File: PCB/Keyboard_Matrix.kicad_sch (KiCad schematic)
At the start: 249 parts

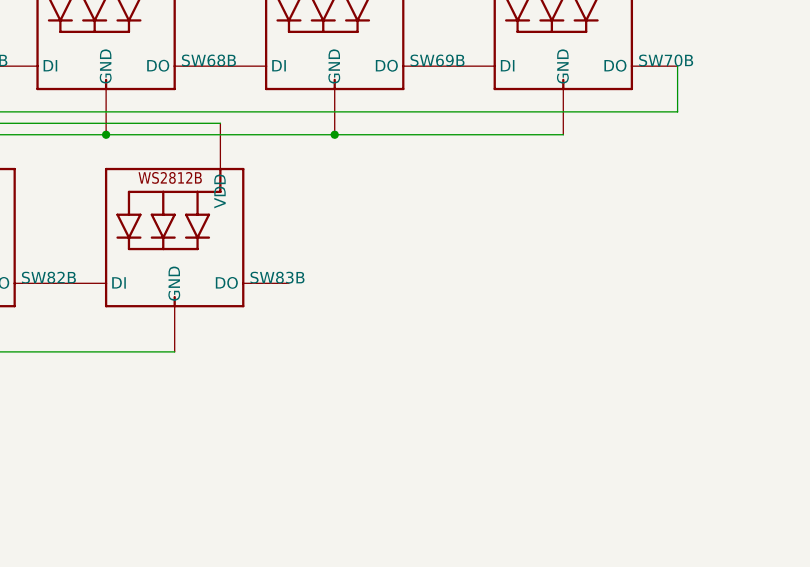
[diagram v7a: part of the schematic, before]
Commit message: PCB is done, still need to do silkscreen
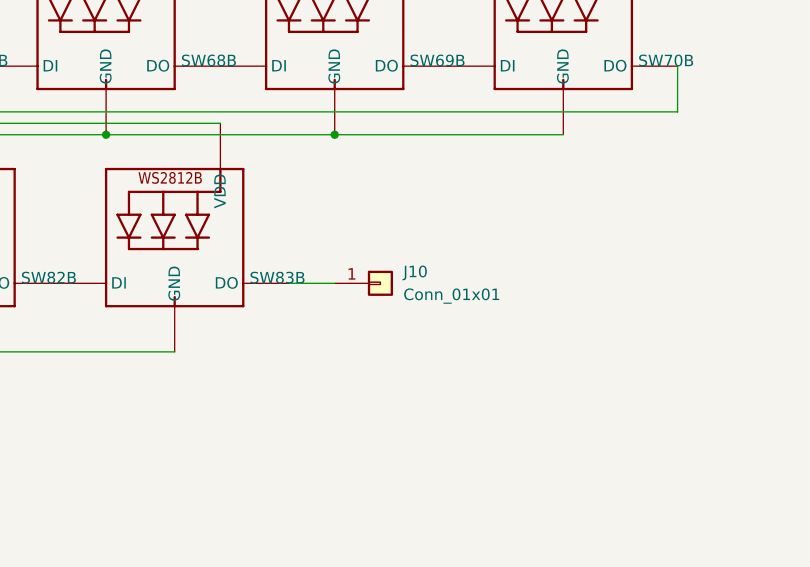
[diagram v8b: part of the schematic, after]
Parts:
- added J10: Conn_01x01, Connector_PinHeader_1.27mm:PinHeader_1x01_P1.27mm_Vertical, symbol Connector_Generic:Conn_01x01
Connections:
- net at SW83.5 (DO): now also J10.1 (Pin_1)
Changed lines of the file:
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@@
 	(wire
 		(pts
+			(xy 313.69 351.79) (xy 318.77 351.79)
+		)
+		(stroke
+			(width 0)
+			(type default)
+		)
+	)
+	(wire
+		(pts
 			(xy 325.12 265.43) (xy 350.52 265.43)
 		)
@@
 					(unit 1)
 				)
+			)
+		)
+	)
+	(symbol
+		(lib_id "Connector_Generic:Conn_01x01")
+		(at 323.85 351.79 0)
+		(unit 1)
+		(exclude_from_sim no)
+		(in_bom yes)
+		(on_board yes)
+		(dnp no)
+		(fields_autoplaced yes)
+		(property "Reference" "J10"
+			(at 326.39 350.5199 0)
+			(effects
+				(font
+					(size 1.27 1.27)
+				)
+				(justify left)
+			)
+		)
+		(property "Value" "Conn_01x01"
+			(at 326.39 353.0599 0)
+			(effects
+				(font
+					(size 1.27 1.27)
+				)
+				(justify left)
+			)
+		)
+		(property "Footprint" "Connector_PinHeader_1.27mm:PinHeader_1x01_P1.27mm_Vertical"
+			(at 323.85 351.79 0)
+			(effects
+				(font
+					(size 1.27 1.27)
+				)
+				(hide yes)
+			)
+		)
+		(property "Datasheet" "~"
+			(at 323.85 351.79 0)
+			(effects
+				(font
+					(size 1.27 1.27)
+				)
+				(hide yes)
+			)
+		)
+		(property "Description" "Generic connector, single row, 01x01, script generated (kicad-library-utils/schlib/autogen/connector/)"
+			(at 323.85 351.79 0)
+			(effects
+				(font
+					(size 1.27 1.27)
+				)
+				(hide yes)
+			)
+		)
+		(pin "1"
+		)
+		(instances
+			(project ""
+				(path "/ea2432c4-eb7a-431a-b465-8c00cfcb4450/17c5c707-0f0f-4f1c-ab03-6f051c1763ce"
+					(reference "J10")
+					(unit 1)
+				)
